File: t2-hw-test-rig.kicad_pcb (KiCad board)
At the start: 2 copper layers, 86.4 x 94 mm, 153 parts, among them J101 CONN_01X02, J102 BARREL_JACK, J103 CONN_01X02, J201 MICROUSB-TH, J202 CONN_01X02, J203 MICROUSB-TH, J204 USB_A_TH, J301 CONN_02x05, 0.05", Q101 pMOS, Q401 CJ2302, Q402 CJ2302, Q403 CJ2302, Q404 CJ2302, Q405 CJ2302 DNP, Q406 CJ2302 DNP, SW301 Switch_DPST, SW302 Switch_DPST, U101 MAX6102, U102 XC6206P332MR-G, U301 ATSAMD21J18A-MUT, U302 AAT4610, U303 AAT4610, U401 MAX9919FASA+, U402 MAX9919FASA+, U403 MAX9919FASA+, U404 MAX9919FASA+, U405 MAX9919FASA+, U501 TSV324IDT, U502 TSV324IDT, U503 TSV324IDT, X301 FC-135

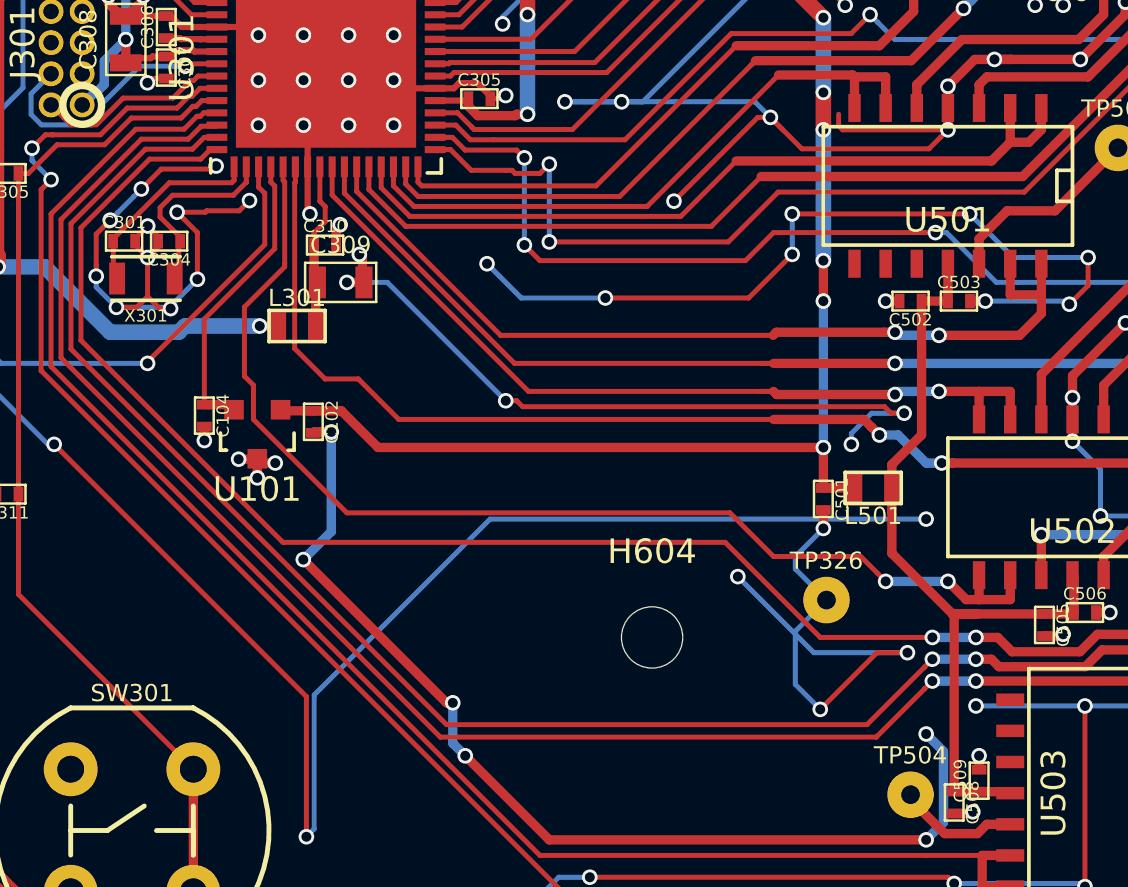
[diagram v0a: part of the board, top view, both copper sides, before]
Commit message: ready to swap the qfn
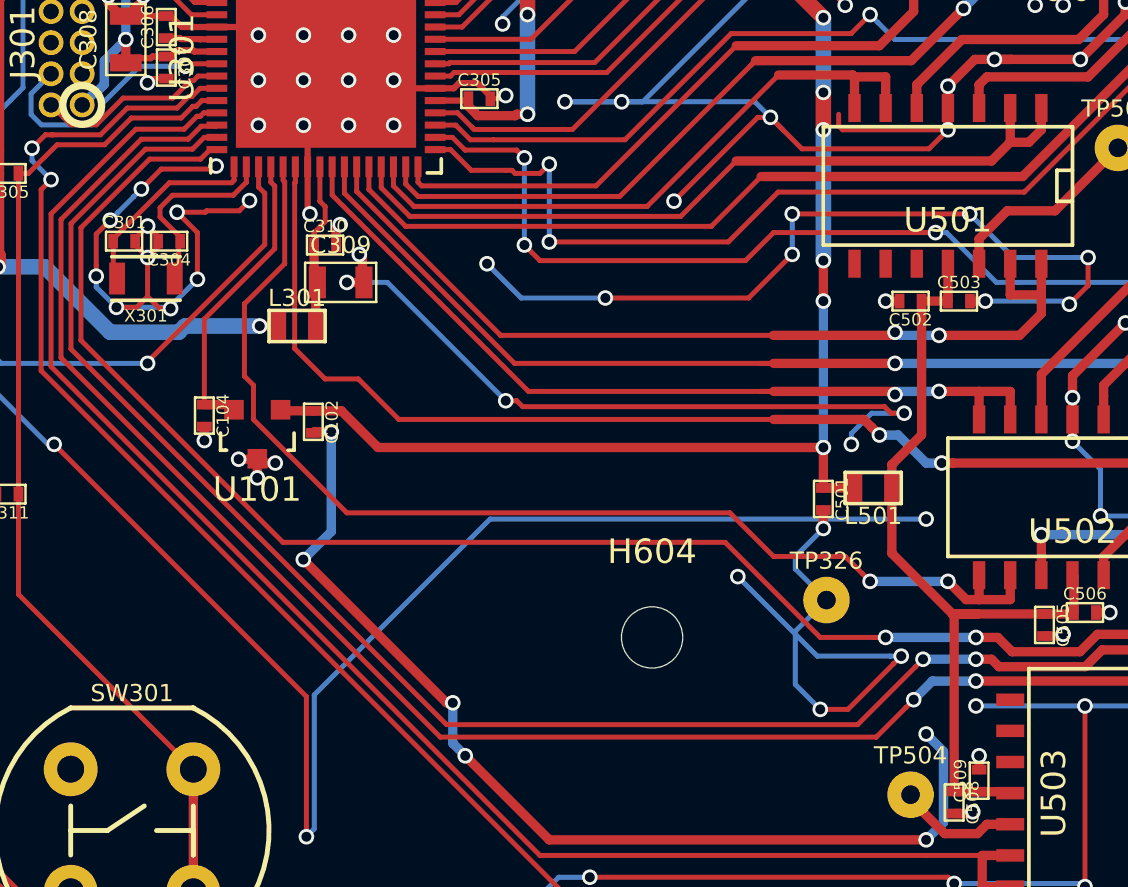
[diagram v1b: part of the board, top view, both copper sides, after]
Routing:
- net GND: track 1405.3 -> 1404.8 mm

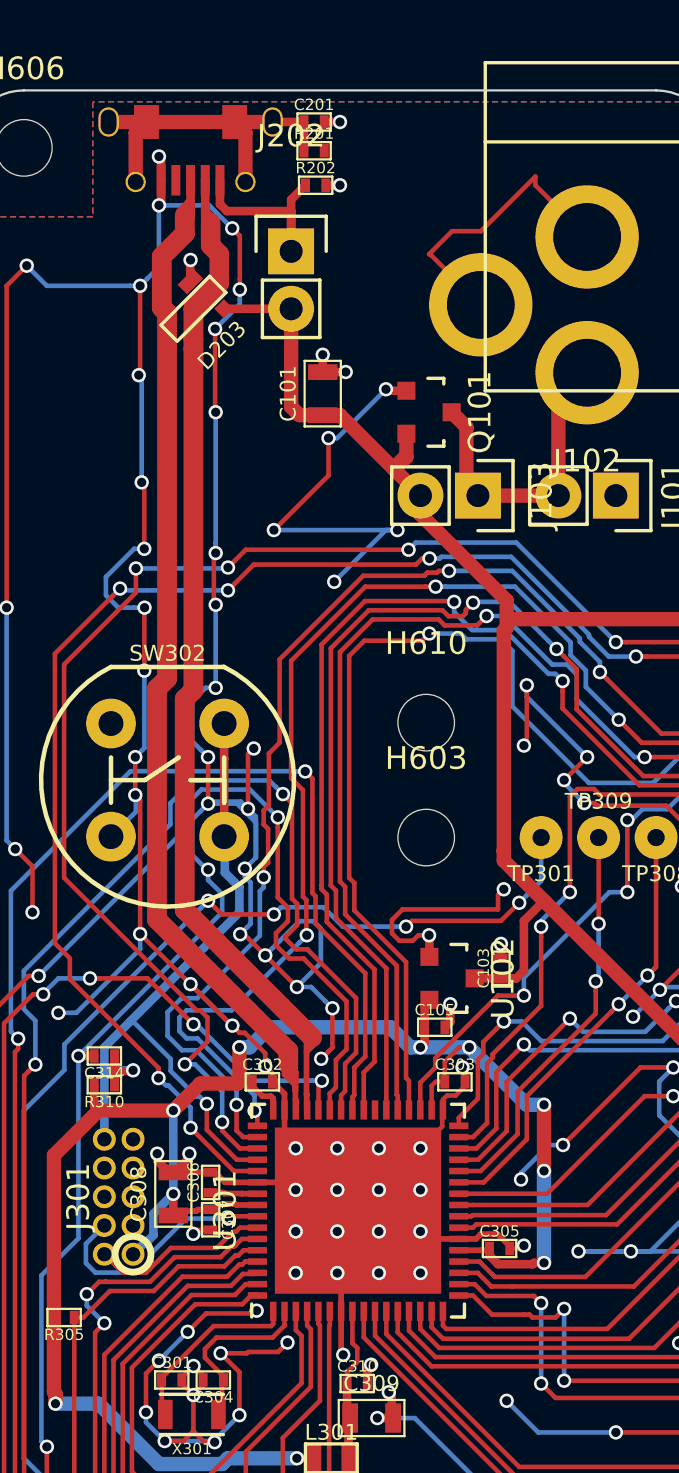
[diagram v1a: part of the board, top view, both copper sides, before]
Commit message: qfn swapped, another mount hole added, passes drc
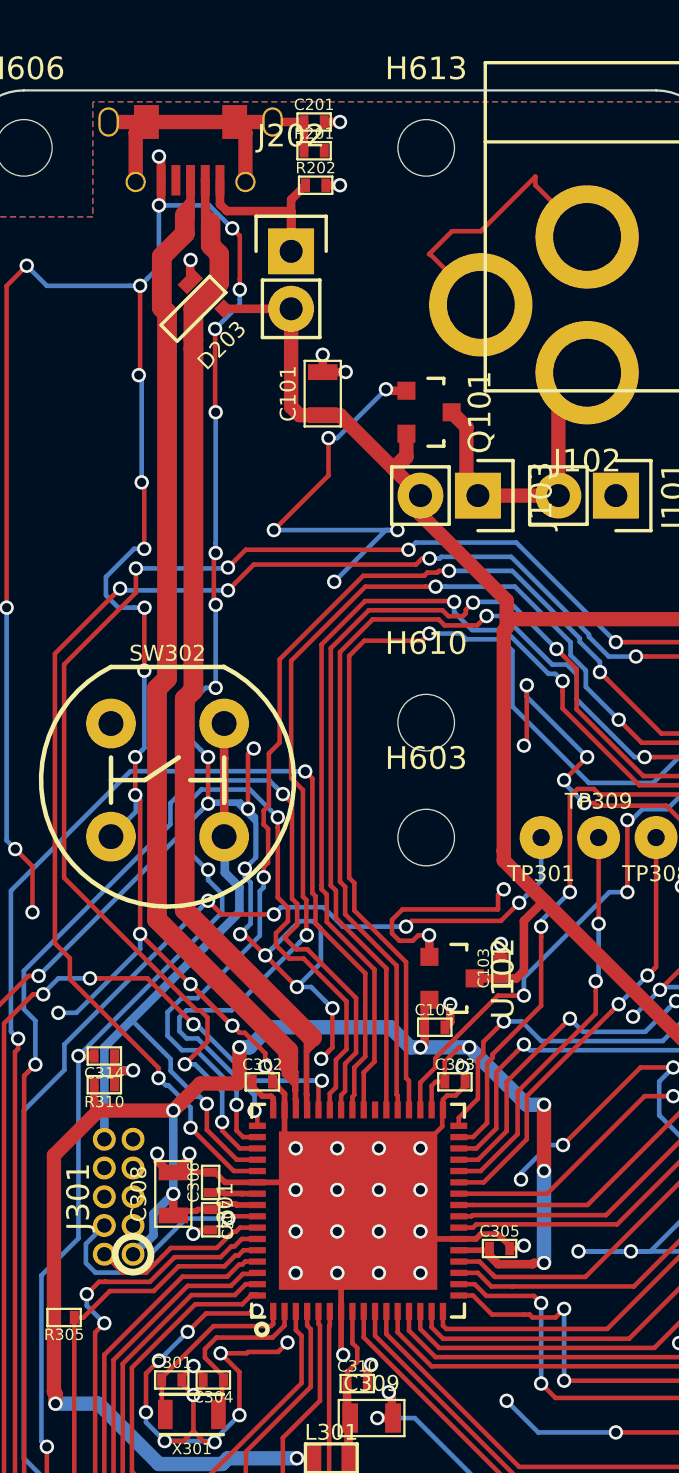
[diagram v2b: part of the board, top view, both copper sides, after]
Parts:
- added H613: M2.5, tm-kicad-lib:MountingHole_2-5mm, F.Cu at (71.1, 61.0)
- U301: footprint Housings_DFN_QFN:QFN-64-1EP_9x9mm_Pitch0.5mm -> tm-kicad-lib:QFN-64-1EP_9x9x0.5-8MILDRC
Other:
- rule via_min_size: 0.4 -> 0.40386

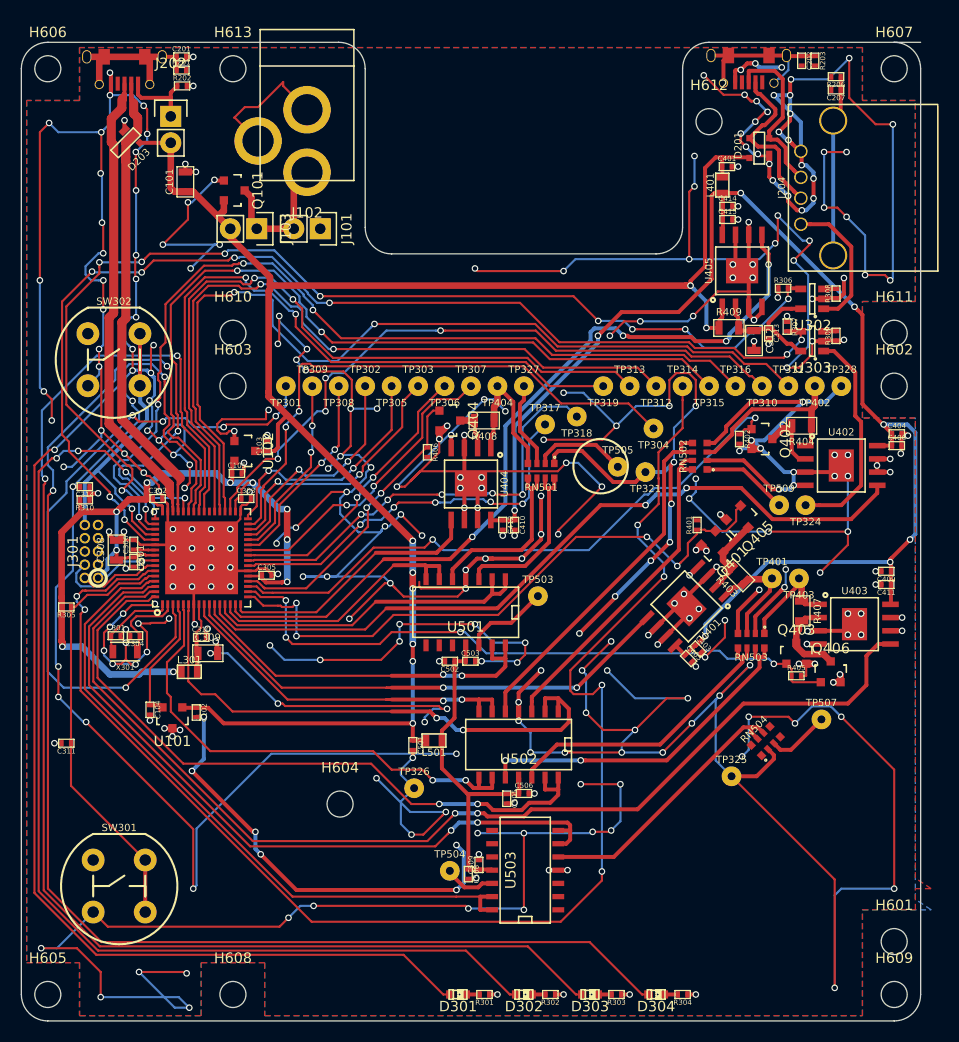
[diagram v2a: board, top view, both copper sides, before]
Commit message: moved usb testpoints
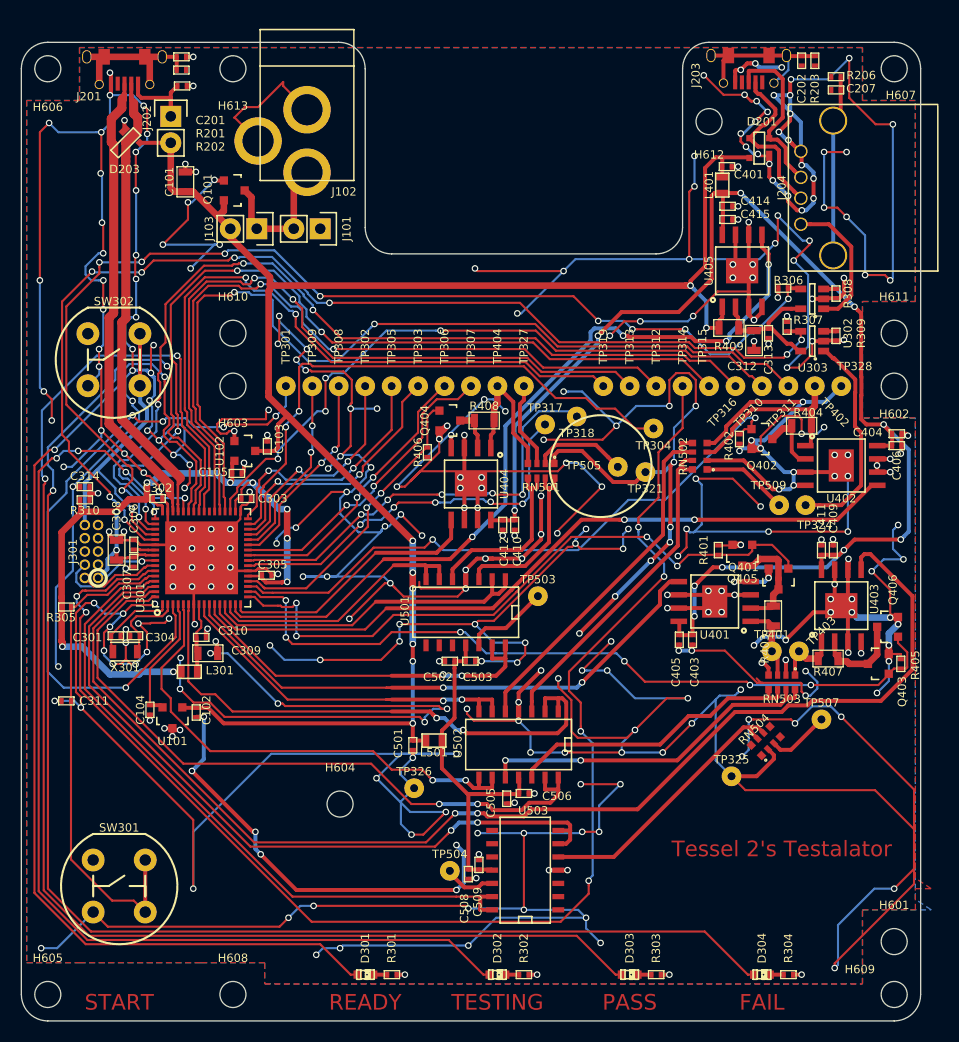
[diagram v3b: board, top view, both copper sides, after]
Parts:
- moved D304 10.3 mm to (121.9, 148.0)
- moved R304 10.3 mm to (124.5, 148.0)
- moved R405 10.1 mm to (135.3, 118.1), turned to 90 degrees
- moved D301 9.09 mm to (83.8, 148.0)
- moved R301 9.09 mm to (86.4, 148.0)
- moved Q403 7.94 mm to (133.1, 118.1), turned to 90 degrees
- moved C411 7.04 mm to (127.6, 107.2), turned to 90 degrees
- moved TP401 7.00 mm to (122.9, 116.9)
- moved TP403 7.00 mm to (125.5, 116.9)
- moved Q406 6.96 mm to (134.0, 114.6), turned to 90 degrees
- moved Q401 6.84 mm to (123.5, 110.0), turned to 180 degrees
- moved C409 5.47 mm to (128.8, 107.2), turned to 90 degrees
- moved R407 5.23 mm to (128.3, 117.6), turned to 0 degrees
- moved R403 5.16 mm to (123.0, 113.5), turned to 90 degrees
- moved RN503 4.96 mm to (123.8, 119.9)
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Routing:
- net GND: track 1404.8 -> 1567.1 mm, vias 336 -> 352
- net I_USB1: track 105.2 -> 119.7 mm
- net USB1_SHORT: track 62.5 -> 74.1 mm, vias 4 -> 6
- net /SAM/READY_LED: track 118.0 -> 108.3 mm
- net /SAM/TEST_START_BUTTON: track 41.8 -> 51.3 mm
- net /SAM/FAIL_LED: track 136.7 -> 146.1 mm
- net I_USB0: track 49.2 -> 54.4 mm
- net UUT_5VUSB1: track 10.7 -> 6.33 mm
- net UUT_5VUSB0: track 11.4 -> 7.35 mm
- net /SAM/PORT_A_MOSI: track 137.2 -> 133.8 mm
- net /SAM/TEST_IN_PROGRESS_LED: track 108.4 -> 105.0 mm
- net /CURRENT/5VUSB0_RS-: track 7.48 -> 10.6 mm
- net USB0_SHORT: track 60.2 -> 63.3 mm
- net /SAM/PASS_LED: track 133.6 -> 136.6 mm
- net I_PA33: track 73.3 -> 70.4 mm
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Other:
- outline, holes or cut-outs redrawn
- board text added: "FAIL"
- board text added: "PASS"
- board text added: "READY"
- board text added: "START"
- board text added: "TESTING"
- board text added: "Tessel 2's Testalator"

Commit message: usb port and barrel jack tweaks
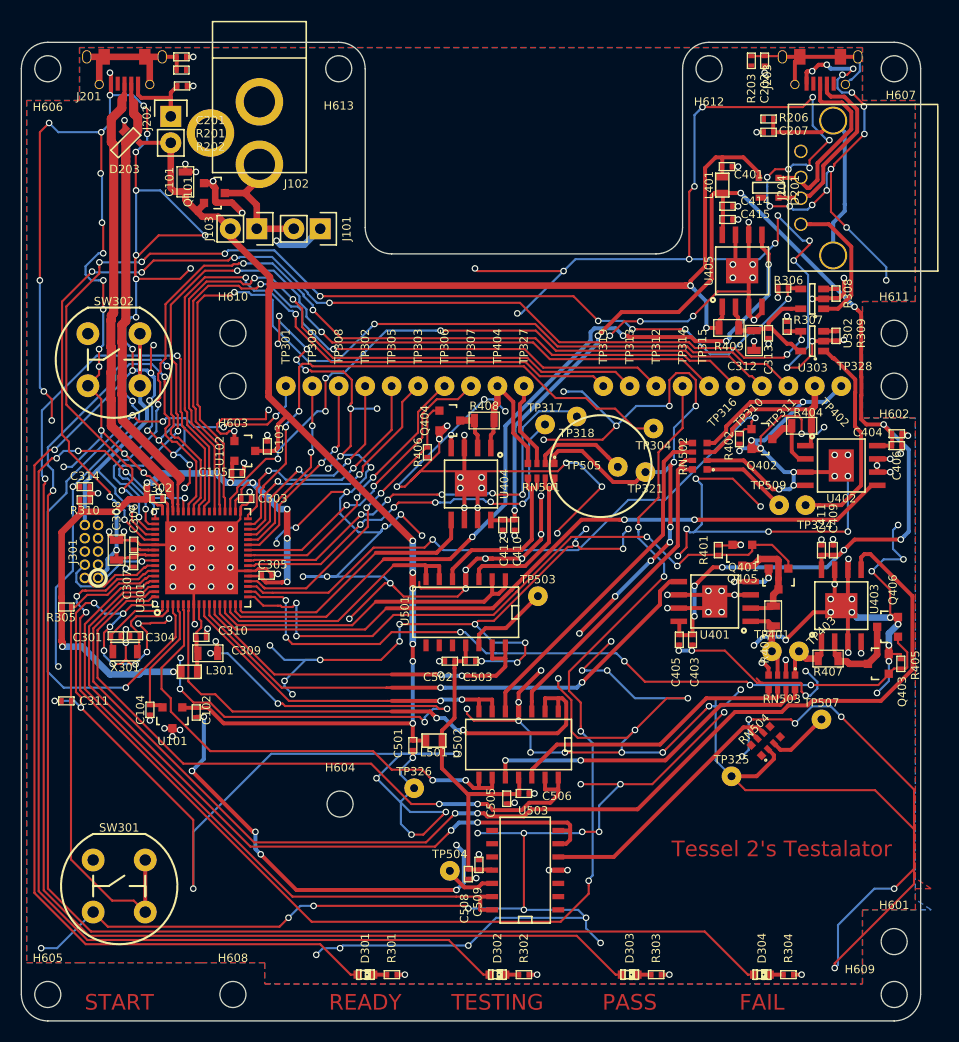
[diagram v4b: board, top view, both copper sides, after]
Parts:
- moved H613 10.2 mm to (81.3, 61.0)
- moved R206 7.65 mm to (122.6, 65.8)
- moved C207 7.65 mm to (122.6, 67.1)
- moved J203 6.86 mm to (127.5, 59.8)
- moved R203 6.10 mm to (120.9, 60.2)
- moved H612 5.08 mm to (116.8, 61.0)
- moved J102 4.64 mm to (73.7, 63.9)
- moved D201 3.91 mm to (122.6, 72.4), turned to 0 degrees
- moved C202 3.56 mm to (122.2, 60.2)
- moved Q101 1.92 mm to (69.3, 72.9)
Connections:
- D201 pad 2: /USB/UUT_USB_D+ -> /USB/UUT_USB_D-
- D201 pad 3: /USB/UUT_USB_D- -> /USB/UUT_USB_D+
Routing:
- net GND: track 1567.1 -> 1561.1 mm, vias 352 -> 344
- net /USB/UUT_USB_SHELL: track 17.5 -> 22.4 mm
- net /USB/UUT_USB_D-: track 16.2 -> 17.7 mm
- net /USB/UUT_USB_D+: track 16.3 -> 17.7 mm

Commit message: still easier access to usb
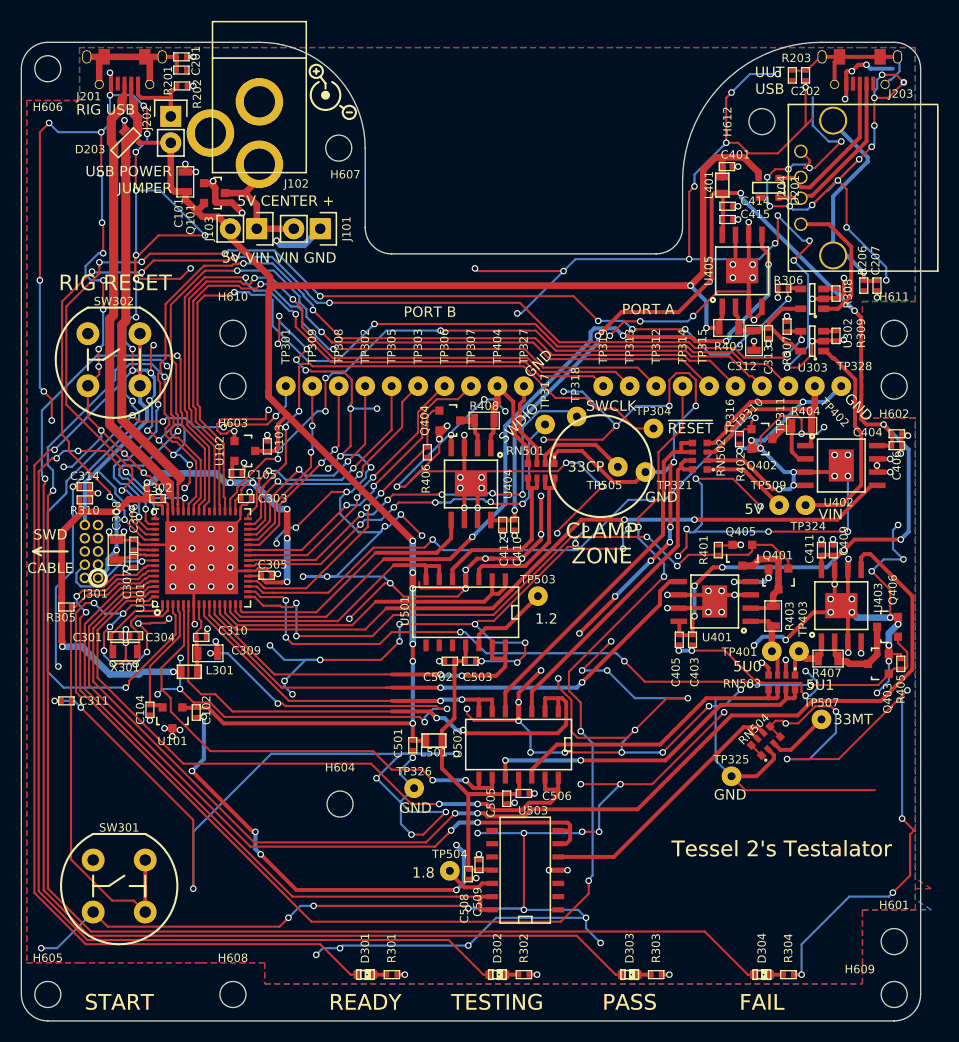
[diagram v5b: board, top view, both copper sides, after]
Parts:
- removed H613: M2.5, tm-kicad-lib:MountingHole_2-5mm
- moved H607 53.9 mm to (81.3, 68.6)
- moved R206 18.4 mm to (131.7, 81.8), turned to 270 degrees
- moved C207 18.0 mm to (133.0, 81.8), turned to 270 degrees
- moved H612 7.18 mm to (121.9, 66.0)
- moved C202 4.18 mm to (126.1, 61.6)
- moved R203 4.18 mm to (124.8, 61.6)
- moved J203 3.81 mm to (131.3, 59.8)
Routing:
- net GND: track 1561.1 -> 1588.3 mm, vias 344 -> 347
- net +5V: track 178.1 -> 180.5 mm
- net /USB/UUT_USB_D+: track 17.7 -> 16.1 mm
- net /USB/UUT_USB_D-: track 17.7 -> 16.3 mm
- net /USB/UUT_USB_SHELL: vias 0 -> 1
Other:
- outline, holes or cut-outs redrawn
- board text added: "1.2"
- board text added: "1.8"
- board text added: "33CP"
- board text added: "33MT"
- board text added: "5U0"
- board text added: "5U1"
- board text added: "5V"
- board text added: "5V CENTER +"
- board text added: "5V VIN VIN GND"
- board text added: "CLAMP ZONE"
- board text added: "GND"
- board text added: "PORT A"
- board text added: "PORT B"
- board text added: "RIG RESET"
- board text added: "RIG USB"
- board text added: "SWCLK"
- board text added: "SWD CABLE"
- board text added: "SWDIO"
- board text added: "USB POWER JUMPER"
- board text added: "UUT USB"
- board text added: "VIN"
- board text added: "~RESET"
